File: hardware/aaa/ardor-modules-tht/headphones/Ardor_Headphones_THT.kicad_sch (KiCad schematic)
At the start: 36 parts, among them J101 5V POWER + ENABLE INPUT, J102 STEREO AUDIO INPUT FROM SOURCE, J602 STEREO HEADPHONE AUDIO OUTPUT, K601 G5V-2-H1 DC5, Q601 2N3904 / E-B-C, U601 LM386N-1/NOPB, U602 LM386N-1/NOPB

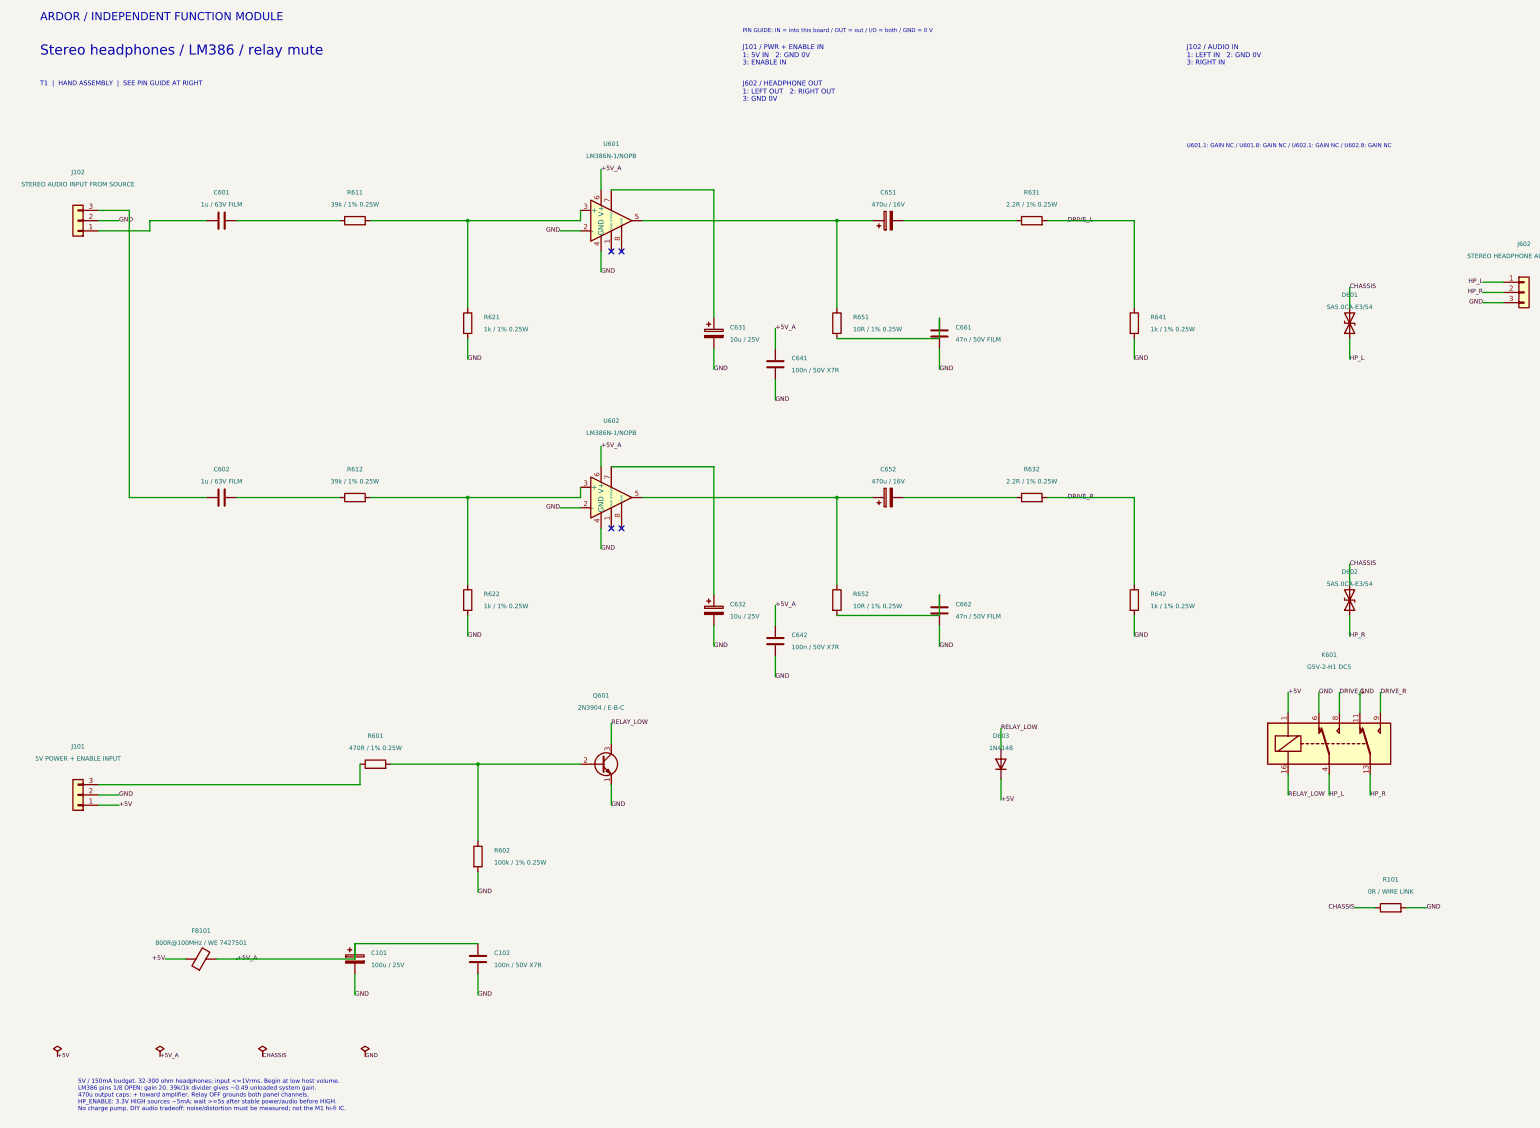
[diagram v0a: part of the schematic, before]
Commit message: feat(hardware): use hand-solderable OPA1656 headphone amplifier
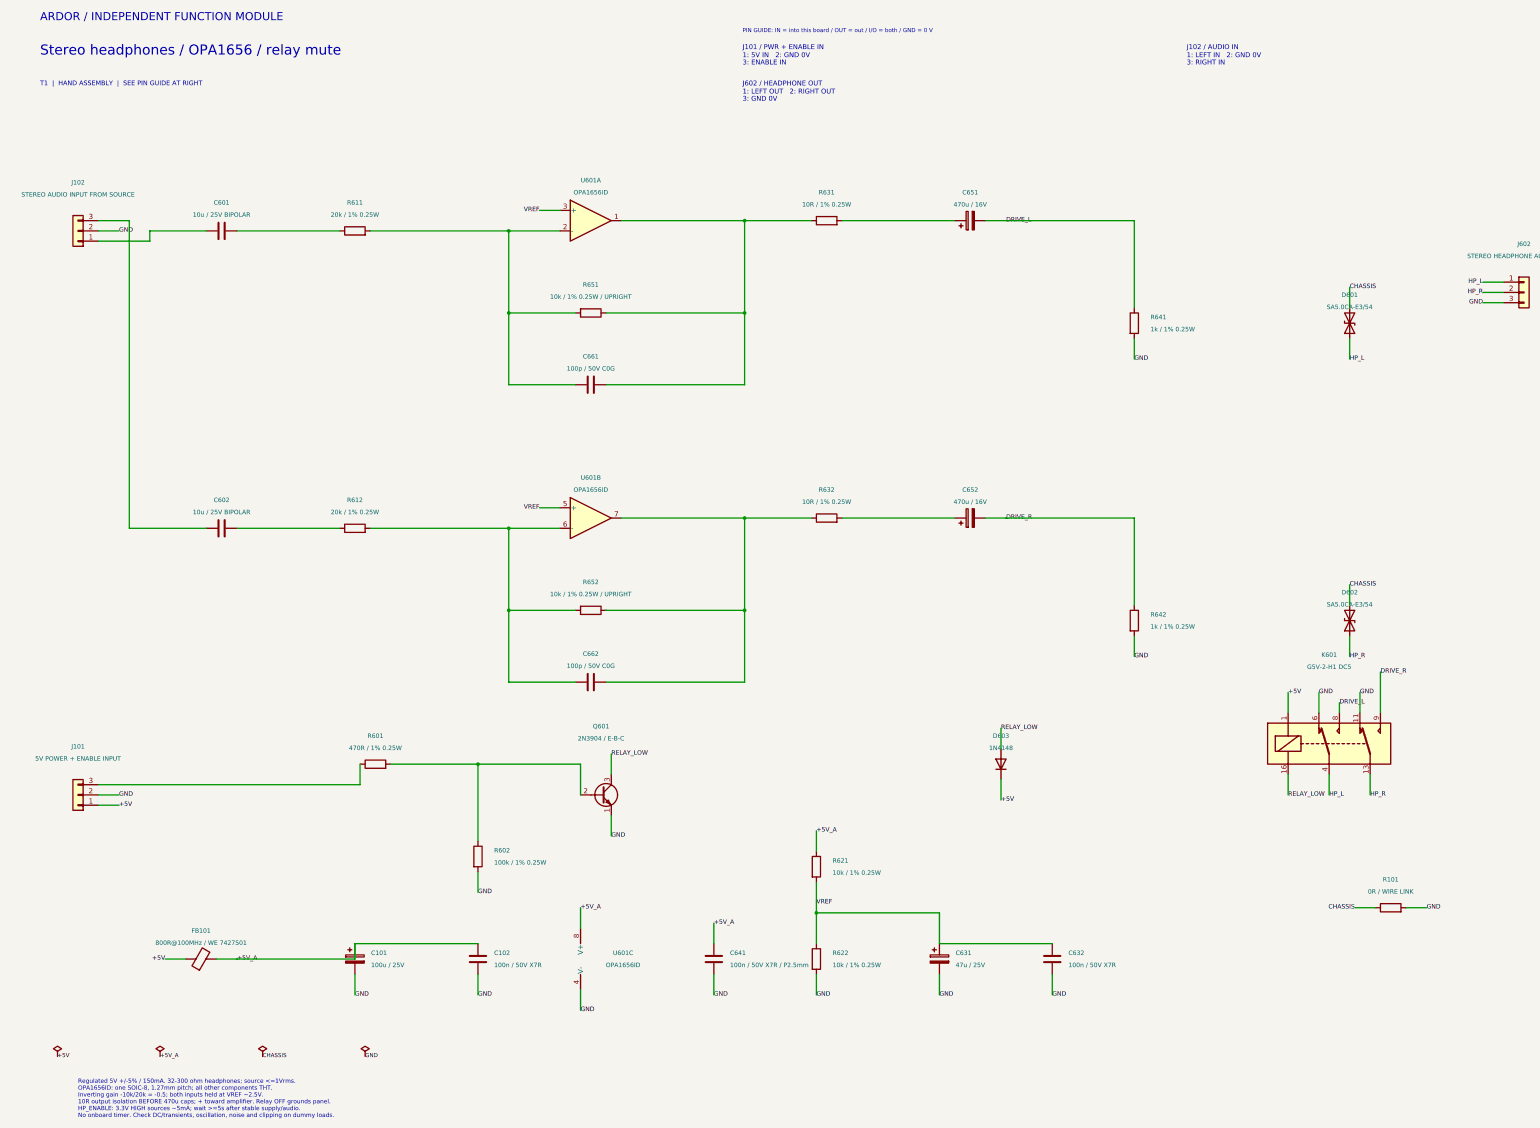
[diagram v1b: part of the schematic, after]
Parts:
- removed C632: 10u / 25V, Capacitor_THT:CP_Radial_D6.3mm_P2.50mm, symbol Ardor:C_Polarized
- removed C642: 100n / 50V X7R, Capacitor_THT:C_Disc_D5.0mm_W2.5mm_P5.00mm, symbol Ardor:C
- removed K601: G5V-2-H1 DC5, Relay_THT:Relay_DPDT_Omron_G5V-2, symbol Ardor:G5V2_THT
- removed U601, U602: LM386N-1/NOPB, Package_DIP:DIP-8_W7.62mm_Socket, symbol Ardor:LM386_THT
- added C632: 100n / 50V X7R, Capacitor_THT:C_Disc_D5.0mm_W2.5mm_P5.00mm, symbol Ardor:C
- added D601: SA5.0CA-E3/54, Diode_THT:D_DO-15_P10.16mm_Horizontal, symbol Ardor:D_TVS
- added R621: 10k / 1% 0.25W, Resistor_THT:R_Axial_DIN0207_L6.3mm_D2.5mm_P10.16mm_Horizontal, symbol Ardor:R
- added unit 2 of U601
- added unit 3 of U601
- C601, C602: value 1u / 63V FILM -> 10u / 25V BIPOLAR; footprint Capacitor_THT:C_Rect_L7.2mm_W3.5mm_P5.00mm_FKS2_FKP2_MKS2_MKP2 -> Ardor_THT:CP_Bipolar_D6.3mm_P2.50mm; MPN 1u / 63V FILM -> Nichicon UES1E100MDM
- C631: value 10u / 25V -> 47u / 25V; MPN 10u / 25V -> 47u / 25V
- C641: value 100n / 50V X7R -> 100n / 50V X7R / P2.5mm; footprint Capacitor_THT:C_Disc_D5.0mm_W2.5mm_P5.00mm -> Capacitor_THT:C_Disc_D3.8mm_W2.6mm_P2.50mm; MPN 100n / 50V X7R -> 100nF 50V X7R radial, D<=3.8mm W<=2.6mm P2.5mm
- C661, C662: value 47n / 50V FILM -> 100p / 50V C0G; footprint Capacitor_THT:C_Rect_L7.2mm_W3.5mm_P5.00mm_FKS2_FKP2_MKS2_MKP2 -> Capacitor_THT:C_Disc_D5.0mm_W2.5mm_P5.00mm; MPN 47n / 50V FILM -> 100p / 50V C0G
- K601: renamed from R652; value 10R / 1% 0.25W -> G5V-2-H1 DC5; footprint Resistor_THT:R_Axial_DIN0207_L6.3mm_D2.5mm_P10.16mm_Horizontal -> Relay_THT:Relay_DPDT_Omron_G5V-2; symbol Ardor:R -> Ardor:G5V2_THT; MPN 10R / 1% 0.25W -> Omron G5V-2-H1 DC5
- R611, R612: value 39k / 1% 0.25W -> 20k / 1% 0.25W; MPN 39k / 1% 0.25W -> 20k / 1% 0.25W
- R622: value 1k / 1% 0.25W -> 10k / 1% 0.25W; MPN 1k / 1% 0.25W -> 10k / 1% 0.25W
- R631, R632: value 2.2R / 1% 0.25W -> 10R / 1% 0.25W; MPN 2.2R / 1% 0.25W -> 10R / 1% 0.25W
- R651: value 10R / 1% 0.25W -> 10k / 1% 0.25W / UPRIGHT; footprint Resistor_THT:R_Axial_DIN0207_L6.3mm_D2.5mm_P10.16mm_Horizontal -> Resistor_THT:R_Axial_DIN0207_L6.3mm_D2.5mm_P2.54mm_Vertical; MPN 10R / 1% 0.25W -> 10k / 1% 0.25W / UPRIGHT
- R652: renamed from D601; value SA5.0CA-E3/54 -> 10k / 1% 0.25W / UPRIGHT; footprint Diode_THT:D_DO-15_P10.16mm_Horizontal -> Resistor_THT:R_Axial_DIN0207_L6.3mm_D2.5mm_P2.54mm_Vertical; symbol Ardor:D_TVS -> Ardor:R; MPN Vishay SA5.0CA-E3/54 -> 10k / 1% 0.25W / UPRIGHT
- U601: renamed from R621; value 1k / 1% 0.25W -> OPA1656ID; footprint Resistor_THT:R_Axial_DIN0207_L6.3mm_D2.5mm_P10.16mm_Horizontal -> Package_SO:SOIC-8_3.9x4.9mm_P1.27mm; symbol Ardor:R -> Ardor:OPA1656; MPN 1k / 1% 0.25W -> Texas Instruments OPA1656ID
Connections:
- net +5V: now also K601.1
- net +5V_A: now also R621.1, U601.8 (V+)
- net CHASSIS: now also D601.2 (A2); no longer R652.2 (A2)
- net DRIVE_L: now also C651.2, K601.8; no longer R631.2
- net DRIVE_R: now also C652.2, K601.9; no longer R632.2
- net GND: now also K601.11, K601.6, C632.2, U601.4 (V-); no longer C661.2, C662.2, U601.2
- net HP_L: now also K601.4, D601.1 (A1); no longer R652.1 (A1)
- net HP_R: now also K601.13
- net RELAY_LOW: now also K601.16
- net at R612.2: now also C662.2, R652.2, U601.6 (-); no longer R622.1
- net at R651.1: now also C661.1, R631.1, U601.1; no longer C651.1
- net at R651.2: now also C661.2, R611.2, U601.2 (-); no longer C661.1
- net VREF: now reaches C631.1
- net VREF: now also R622.1, U601.3 (+), C632.1, R621.2, U601.5 (+)
- net at C652.1: now also R632.2; no longer K601.1
- net at R632.1: now also C662.1, R652.1, U601.7; no longer C652.2
- new net: C651.1, R631.2
- no-connect marks 4 -> 0
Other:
- note added: "Regulated 5V +/-5% / 150mA. 32-300 ohm headphones; source <=1Vrms. OPA1656ID: one SOIC-8, 1.27mm pitch; all other components THT. Inverting gain -10k/20k = -0.5; both inputs held at VREF ~2.5V. 10R output isolation BEFORE 470u caps; + toward amplifier. Relay OFF grounds panel. HP_ENABLE: 3.3V HIGH sources ~5mA; wait >=5s after stable supply/audio. No onboard timer. Check DC/transients, oscillatio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"
- note added: "Stereo headphones / OPA1656 / relay mute"
- note removed: "5V / 150mA budget. 32-300 ohm headphones; input <=1Vrms. Begin at low host volume. LM386 pins 1/8 OPEN: gain 20. 39k/1k divider gives ~0.49 unloaded system gain. 470u output caps: + toward amplifier. Relay OFF grounds both panel channels. HP_ENABLE: 3.3V HIGH sources ~5mA; wait >=5s after stable power/audio before HIGH. No charge pump. DIY audio tradeoff: noise/distortion must be measured; not th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"
- note removed: "Stereo headphones / LM386 / relay mute"
- note removed: "U601.1: GAIN NC / U601.8: GAIN NC / U602.1: GAIN NC / U602.8: GAIN NC"
- title: Stereo headphones / LM386 / relay mute -> Stereo headphones / OPA1656 / relay mute
- moved on the sheet: C601, J102, R611

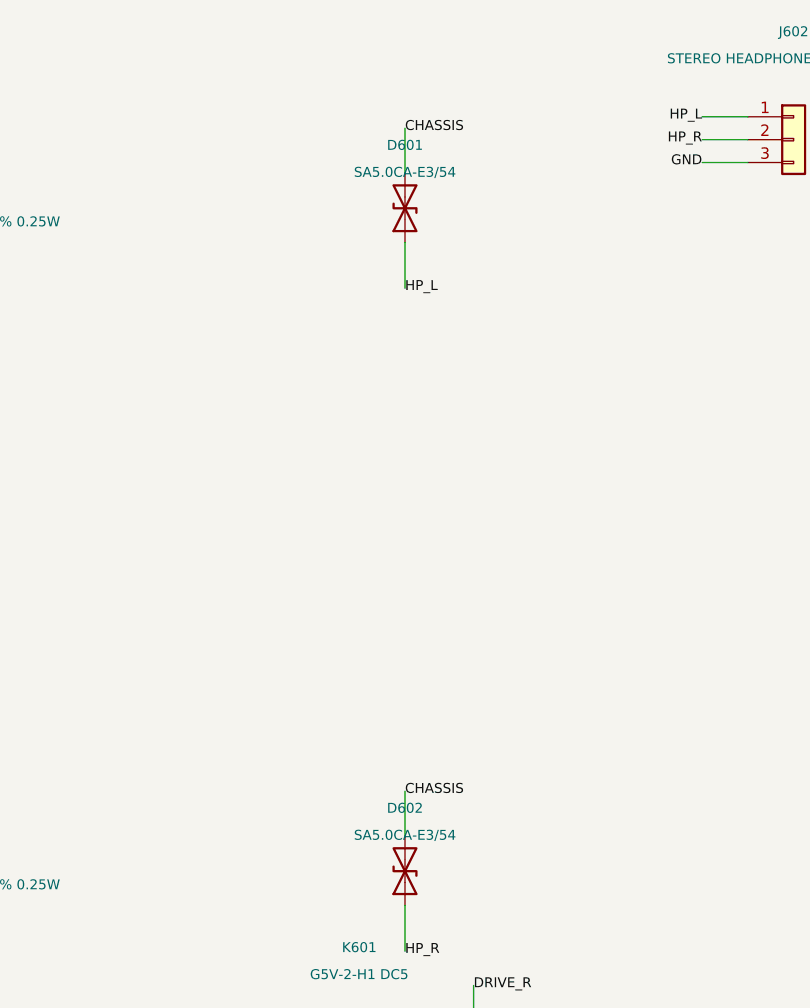
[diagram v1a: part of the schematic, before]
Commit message: fix(hardware): use Hestore TVS diodes in hand-assembly modules
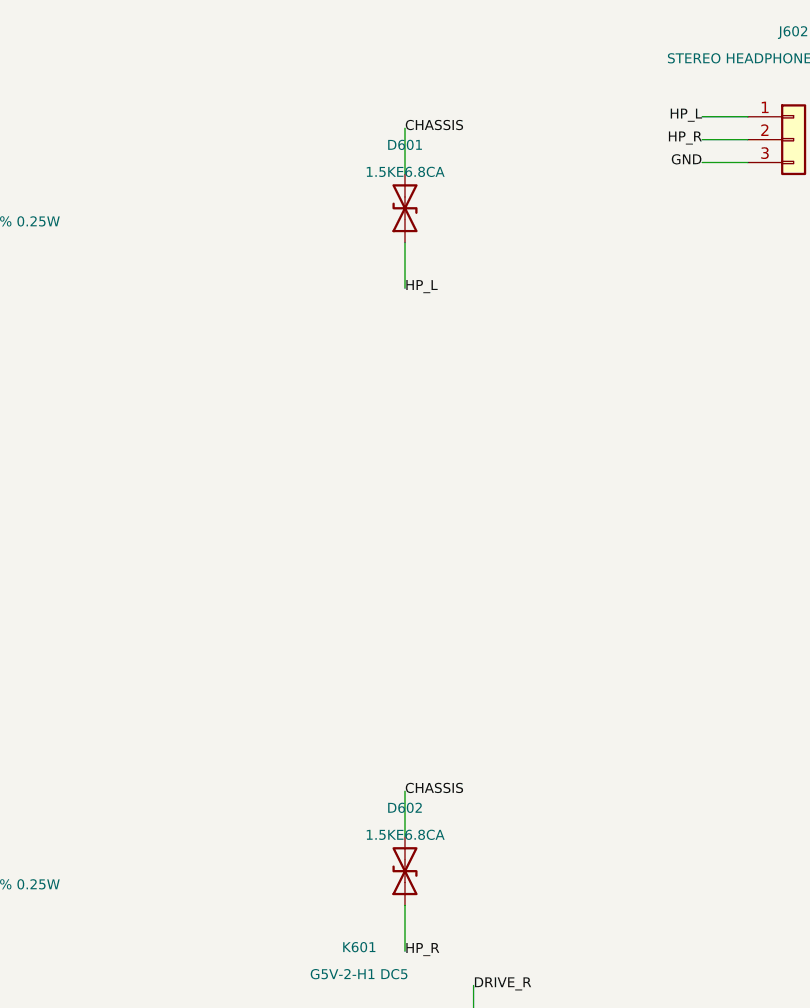
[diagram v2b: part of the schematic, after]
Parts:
- D601, D602: value SA5.0CA-E3/54 -> 1.5KE6.8CA; footprint Diode_THT:D_DO-15_P10.16mm_Horizontal -> Ardor_THT:D_TVS_DC_1.5KE_P15.24mm; MPN Vishay SA5.0CA-E3/54 -> DC Components 1.5KE6.8CA (HESTORE 100.430.71)

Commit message: feat(hardware): compact layouts and adopt Hestore module packages
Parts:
- C601, C602: value 10u / 25V BIPOLAR -> 10u / 50V BIPOLAR; footprint Ardor_THT:CP_Bipolar_D6.3mm_P2.50mm -> Ardor_THT:CP_Bipolar_Nichicon_D8.0mm_P3.50mm; MPN Nichicon UES1E100MDM -> Nichicon UES1H100MPM (HESTORE 100.524.69)
